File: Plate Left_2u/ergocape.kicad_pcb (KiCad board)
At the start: 2 copper layers, 183.2 x 140.8 mm, 42 parts

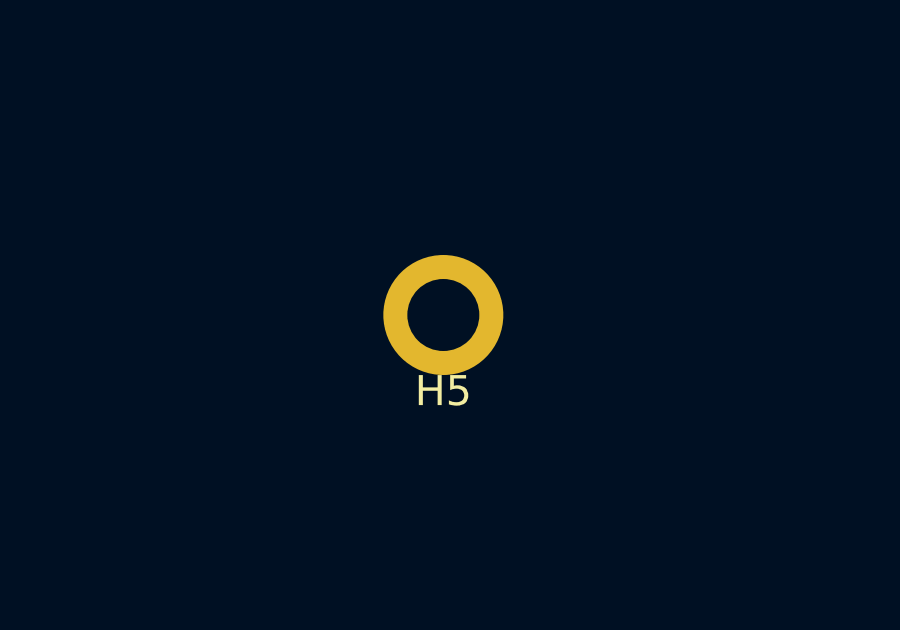
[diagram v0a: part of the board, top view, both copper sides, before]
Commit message: Change in layout and design, remove atmega32u4
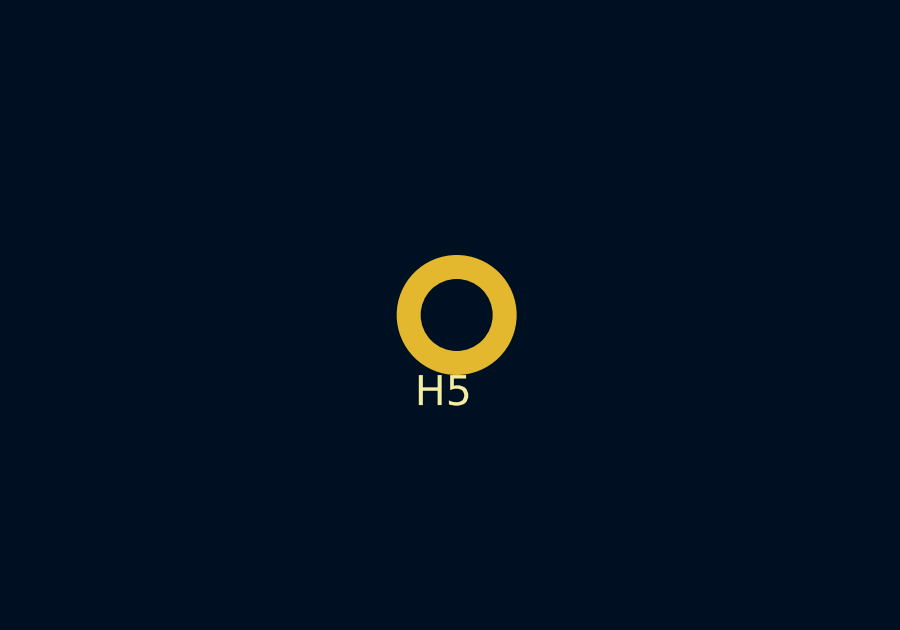
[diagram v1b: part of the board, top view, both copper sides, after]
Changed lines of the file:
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@@
     (mod_text_size 1 1)
     (mod_text_width 0.15)
-    (pad_size 5.2 5.2)
-    (pad_drill 4.7)
+    (pad_size 4 4)
+    (pad_drill 2.4)
     (pad_to_mask_clearance 0.051)
     (solder_mask_min_width 0.25)
@@
       (effects (font (size 1 1) (thickness 0.15)))
     )
-    (pad "" thru_hole circle (at 0 0) (size 4 4) (drill 2.4) (layers *.Cu *.Mask))
+    (pad "" thru_hole circle (at 0.4445 0) (size 4 4) (drill 2.4) (layers *.Cu *.Mask))
   )
   (module usbc_footprint:mount_hole_2.4x4 (layer F.Cu)

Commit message: cleanup and finish the case files
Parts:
- added K_XTRA1: KEYSW, usbc_footprint:slotMX100, F.Cu at (46.1, 39.7)
- H1, H10, H11, H12, H2, H3, H5, H6, H8, H9: footprint usbc_footprint:mount_hole_2.4x4 -> acheron_MountingHoles:MountingHole_2.5x4.0mm
- K_1, K_2, K_3, K_4, K_5, K_A1, K_ALT1, K_B1, K_BOT_1U_1, K_BOT_1U_2, K_C1, K_CAPS1, K_CTRL1, K_D1, K_E1, K_ESC1, K_F1, K_G1, K_Q1, K_R1, K_S1, K_T1, K_TAB1, K_TH_1U_1, K_TH_1U_2, K_V1, K_W1, K_WIN1, K_X1, K_Z1: footprint acheron_SwitchSlots:slotMX100 -> usbc_footprint:slotMX100
- K_SHIFT1, K_THUMB_2U1: footprint acheron_SwitchSlots:slotMX200 -> usbc_footprint:slotMX200
- moved H10 16.1 mm to (39.6, 60.5)
- moved H11 14.2 mm to (39.9, 20.2)
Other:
- outline, holes or cut-outs redrawn

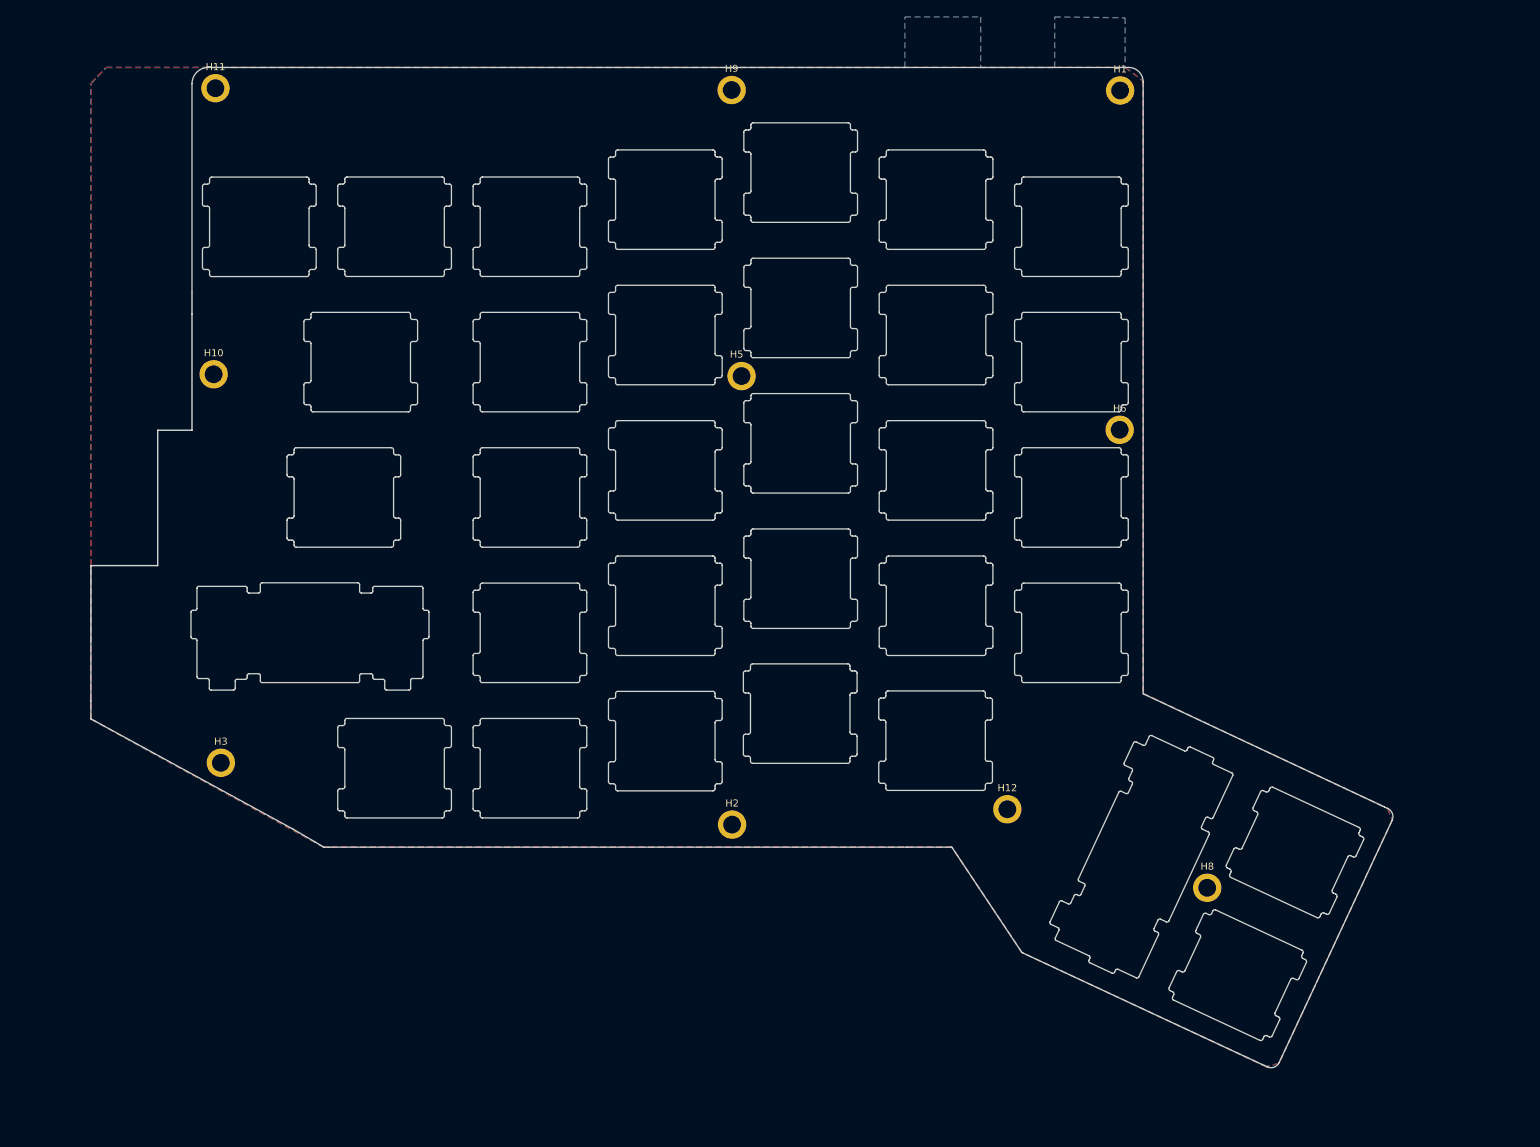
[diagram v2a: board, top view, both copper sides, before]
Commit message: finalize plate and mounting holes
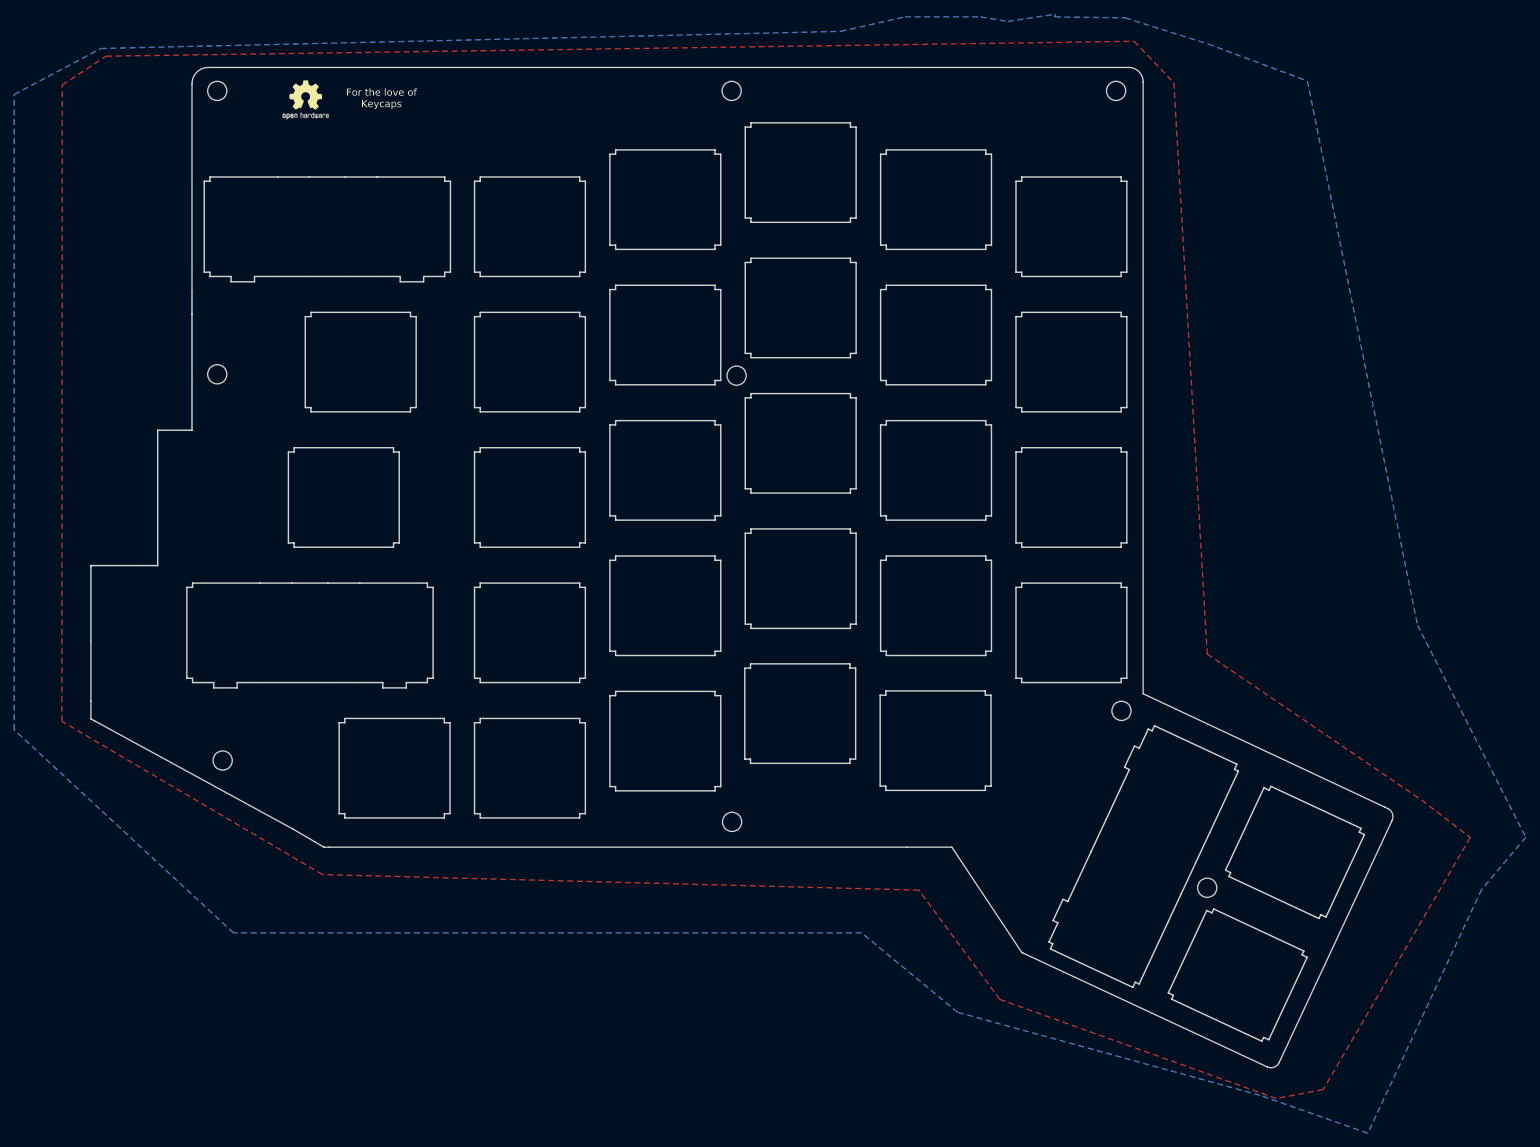
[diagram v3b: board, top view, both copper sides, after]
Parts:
- removed H6: MountingHole, acheron_MountingHoles:MountingHole_2.5x4.0mm
- removed K_XTRA1: KEYSW, usbc_footprint:slotMX100
- added REF**: OSHW-Logo2_7.3x6mm_SilkScreen, logo_lib:OSHW-Logo2_7.3x6mm_SilkScreen, B.Cu at (52.6, 21.8)
- added REF**: OSHW-Logo2_7.3x6mm_SilkScreen, logo_lib:OSHW-Logo2_7.3x6mm_SilkScreen, F.Cu at (52.6, 21.8)
- H1, H10, H11, H12, H2, H3, H5, H8, H9: footprint acheron_MountingHoles:MountingHole_2.5x4.0mm -> MountingHole:MountingHole_2.7mm_M2.5
- K_1, K_2, K_3, K_4, K_5, K_A1, K_ALT1, K_B1, K_BOT_1U_1, K_BOT_1U_2, K_C1, K_CAPS1, K_CTRL1, K_D1, K_E1, K_F1, K_G1, K_Q1, K_R1, K_S1, K_T1, K_TAB1, K_TH_1U_1, K_TH_1U_2, K_V1, K_W1, K_WIN1, K_X1, K_Z1: footprint usbc_footprint:slotMX100 -> usbc_footprint:1u_uni
- K_ESC1: footprint usbc_footprint:slotMX100 -> usbc_footprint:mixed_2u_uni_centered
- K_SHIFT1, K_THUMB_2U1: footprint usbc_footprint:slotMX200 -> usbc_footprint:mixed_2u_uni_centered
- moved H12 21.2 mm to (167.4, 107.8)
- moved K_ESC1 9.46 mm to (55.6, 39.7)
- moved H1 0.58 mm to (166.6, 20.6)
- moved H10 0.51 mm to (40.1, 60.5)
- moved H11 0.46 mm to (40.1, 20.6)
- moved H3 0.41 mm to (40.9, 114.8)
- moved H2 0.38 mm to (112.6, 123.4)
- moved H9 0.13 mm to (112.5, 20.6)
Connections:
- H9 pad 1: GND -> (no net)
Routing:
- added copper zone on B.Cu, net (none)
- added copper zone on F.Cu, net (none)
- removed copper zone on B.Cu, net GND
- removed copper zone on F.Cu, net GND
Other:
- outline, holes or cut-outs redrawn
- board text added: "For the love of Keycaps"
